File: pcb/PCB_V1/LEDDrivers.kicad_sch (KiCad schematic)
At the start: 65 parts, among them J711 LED +/- (return isolated), J721 LED +/- (return isolated), J731 LED +/- (return isolated), Q711 SiR106ADP-T1-RE3, Q721 DMT10H009LK3-13, Q731 DMT10H009LK3-13, U700 SN74LVC1G08DBVR, U710 AL8853S-13, U720 AL8853S-13, U730 AL8853S-13

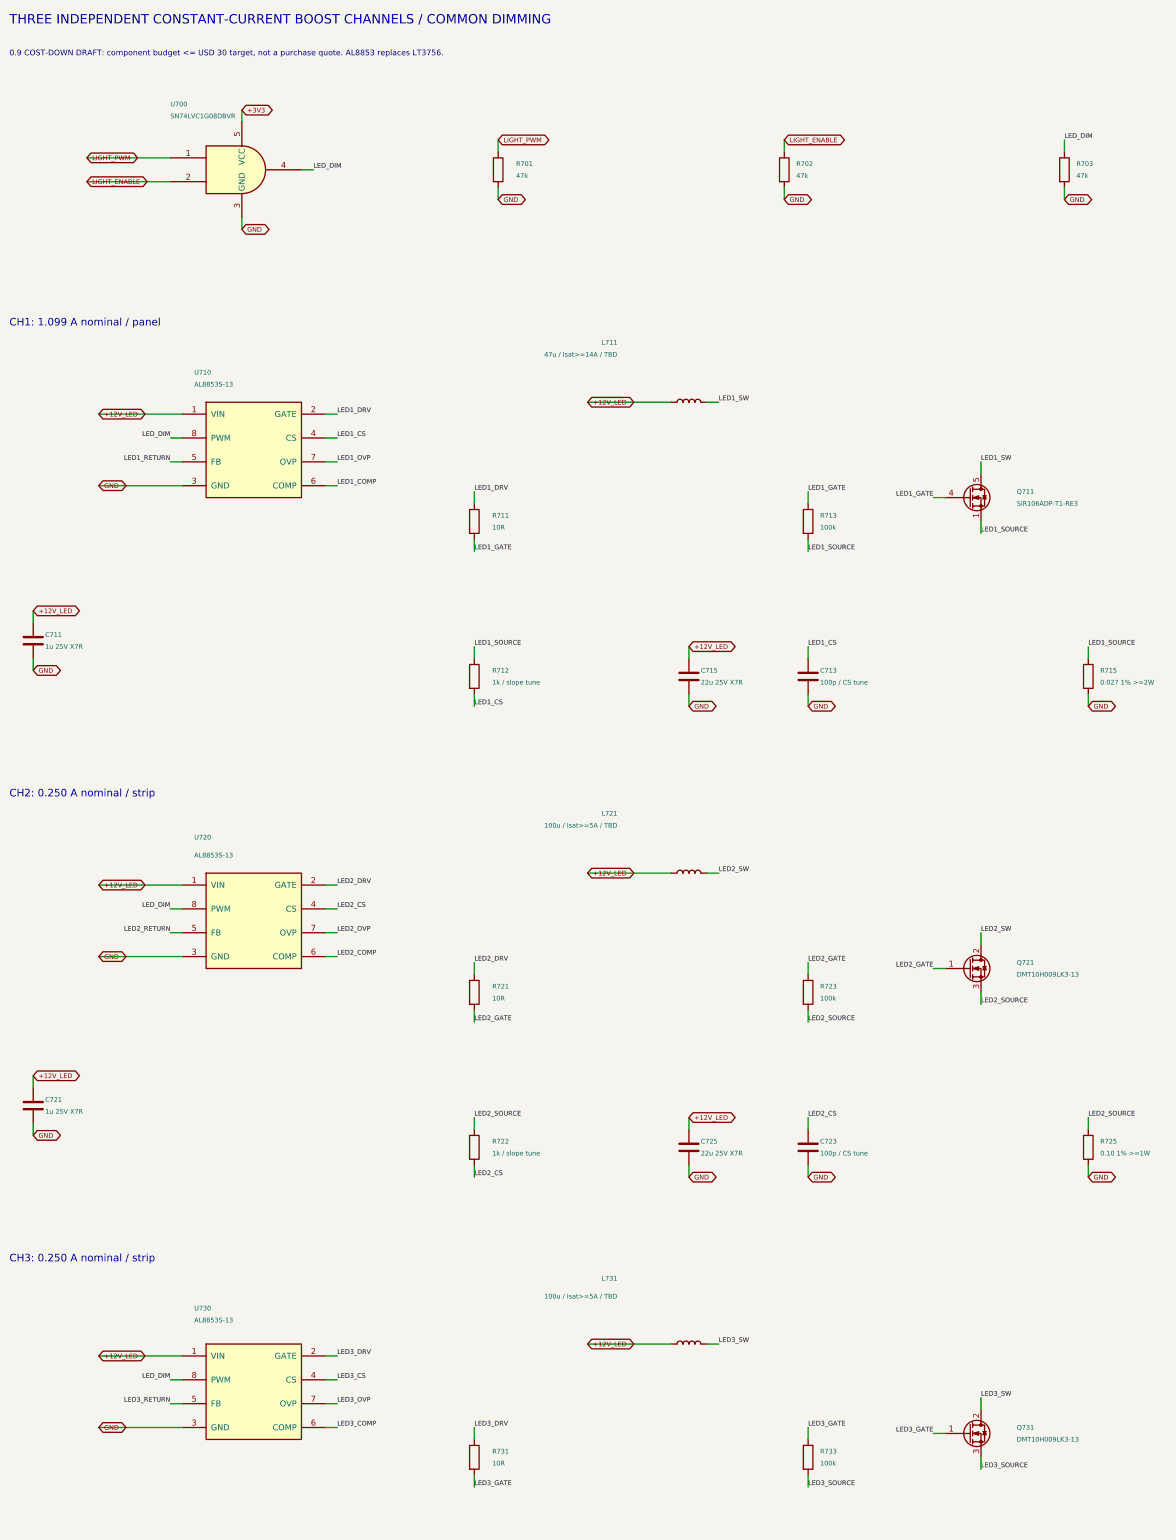
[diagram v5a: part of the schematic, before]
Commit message: pcb: adopt DS3231MZ RTC and compact TI strip MOSFETs
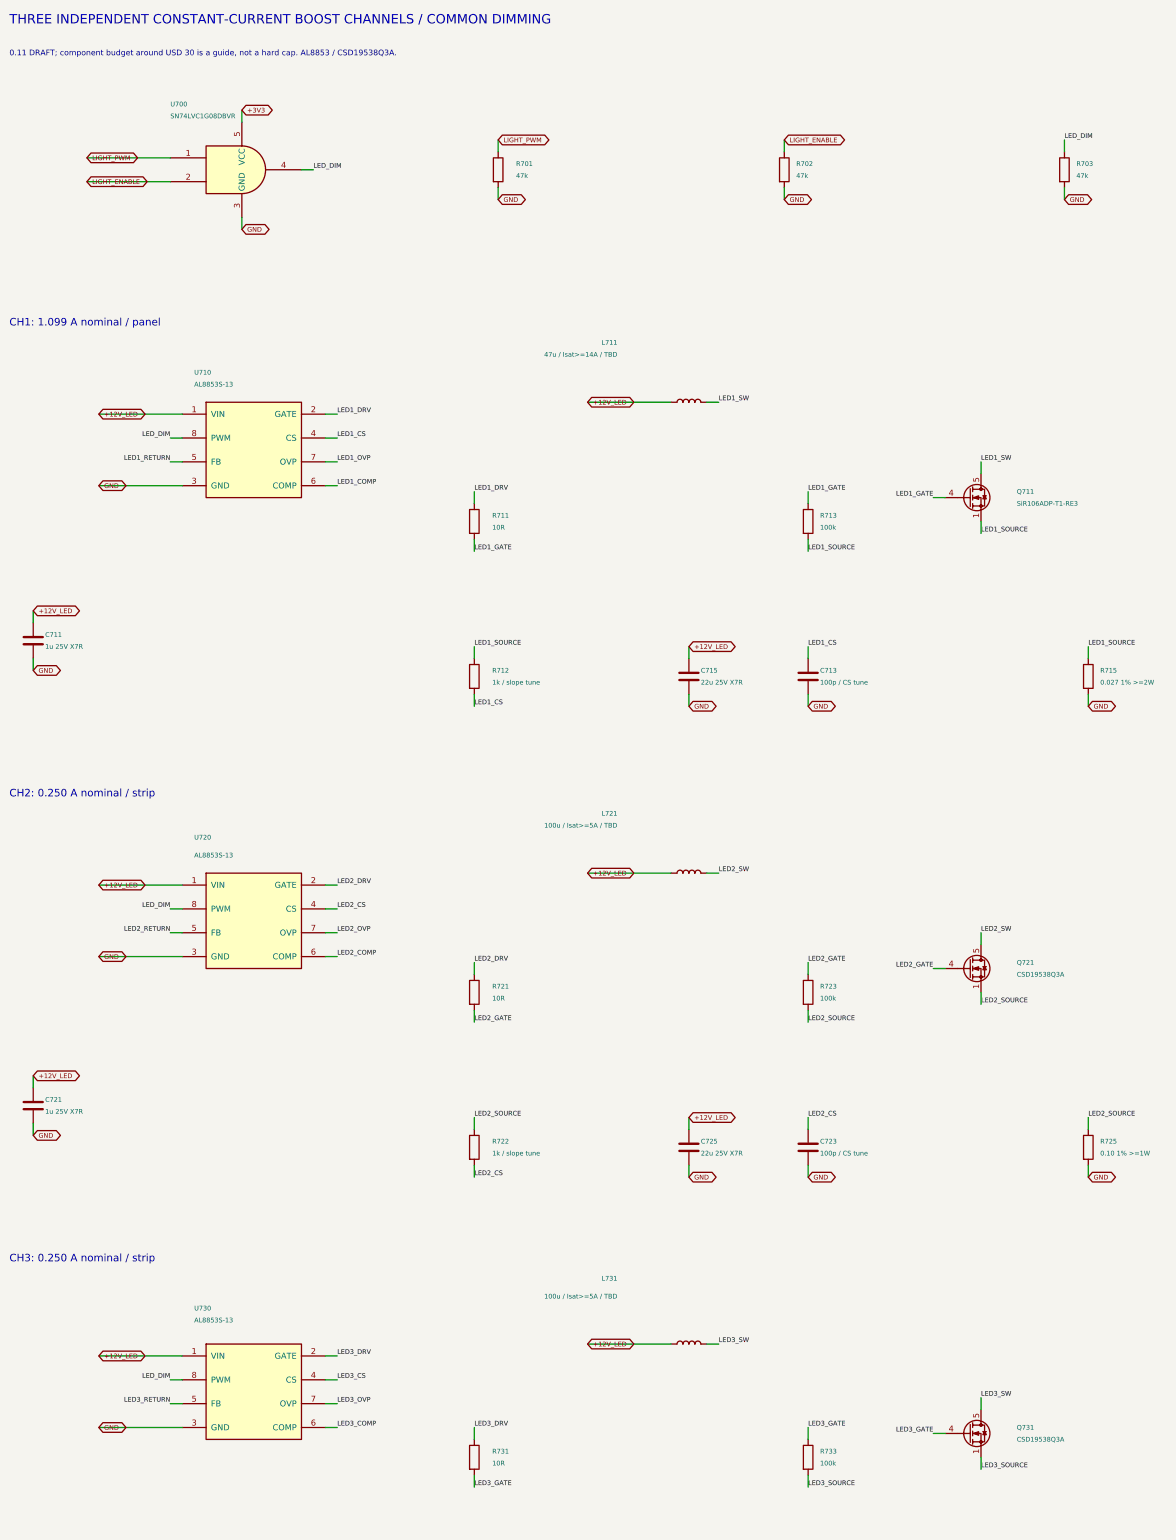
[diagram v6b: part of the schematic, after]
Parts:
- Q721, Q731: value DMT10H009LK3-13 -> CSD19538Q3A; footprint GrowBox:Diodes_TO252_DMT10H009LK3 -> GrowBox:TI_DNH0008A_CSD19538Q3A; symbol GrowBox:DMT10H009LK3 -> GrowBox:CSD19538Q3A
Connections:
- net LED2_GATE: now also Q721.4 (G); no longer Q721.1 (G)
- net LED2_SOURCE: now also Q721.1 (S), Q721.2 (S)
- net LED2_SW: now also Q721.5 (D); no longer Q721.2 (D)
- net LED3_GATE: now also Q731.4 (G); no longer Q731.1 (G)
- net LED3_SOURCE: now also Q731.1 (S), Q731.2 (S)
- net LED3_SW: now also Q731.5 (D); no longer Q731.2 (D)
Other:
- note added: "0.11 DRAFT; component budget around USD 30 is a guide, not a hard cap. AL8853 / CSD19538Q3A."
- note removed: "0.9 COST-DOWN DRAFT: component budget <= USD 30 target, not a purchase quote. AL8853 replaces LT3756."
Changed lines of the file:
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@@
 		(title "07 - AL8853 cost-down LED drivers")
 		(date "2026-09-27")
-		(rev "0.10-DRAFT")
+		(rev "0.11-DRAFT")
 		(company "GrowBox controller")
 		(comment 1 "AL8853 cost-down prototype; not fabrication ready")
@@
 		)
 	)
-	(text "0.9 COST-DOWN DRAFT: component budget <= USD 30 target, not a purchase quote. AL8853 replaces LT3756."
+	(text "0.11 DRAFT; component budget around USD 30 is a guide, not a hard cap. AL8853 / CSD19538Q3A."
 		(exclude_from_sim no)
 		(at 20.32 22.86 0)
@@
 	)
 	(symbol
-		(lib_id "GrowBox:DMT10H009LK3")
+		(lib_id "GrowBox:CSD19538Q3A")
 		(at 224.79 218.44 0)
 		(unit 1)
@@
 			)
 		)
-		(property "Value" "DMT10H009LK3-13"
+		(property "Value" "CSD19538Q3A"
 			(at 234.95 219.71 0)
 			(show_name no)
@@
 			)
 		)
-		(property "Footprint" "GrowBox:Diodes_TO252_DMT10H009LK3"
+		(property "Footprint" "GrowBox:TI_DNH0008A_CSD19538Q3A"
 			(at 224.79 218.44 0)
 			(hide yes)
@@
 			)
 		)
-		(property "Datasheet" "https://www.diodes.com/datasheet/download/DMT10H009LK3.pdf"
+		(property "Datasheet" "https://www.ti.com/lit/ds/symlink/csd19538q3a.pdf"
 			(at 224.79 218.44 0)
 			(hide yes)
@@
 			)
 		)
-		(pin "1"
-		)
-		(pin "2"
-		)
-		(pin "3"
-		)
 		(instances
 			(project "PCB_V1"
@@
 			)
 		)
+		(pin "1"
+		)
+		(pin "2"
+		)
+		(pin "3"
+		)
+		(pin "4"
+		)
+		(pin "5"
+		)
 	)
 	(symbol
@@
 	)
 	(symbol
-		(lib_id "GrowBox:DMT10H009LK3")
+		(lib_id "GrowBox:CSD19538Q3A")
 		(at 224.79 317.5 0)
 		(unit 1)
@@
 			)
 		)
-		(property "Value" "DMT10H009LK3-13"
+		(property "Value" "CSD19538Q3A"
 			(at 234.95 318.77 0)
 			(show_name no)
@@
 			)
 		)
-		(property "Footprint" "GrowBox:Diodes_TO252_DMT10H009LK3"
+		(property "Footprint" "GrowBox:TI_DNH0008A_CSD19538Q3A"
 			(at 224.79 317.5 0)
 			(hide yes)
@@
 			)
 		)
-		(property "Datasheet" "https://www.diodes.com/datasheet/download/DMT10H009LK3.pdf"
+		(property "Datasheet" "https://www.ti.com/lit/ds/symlink/csd19538q3a.pdf"
 			(at 224.79 317.5 0)
 			(hide yes)
@@
 			)
 		)
-		(pin "1"
-		)
-		(pin "2"
-		)
-		(pin "3"
-		)
 		(instances
 			(project "PCB_V1"
@@
 			)
 		)
+		(pin "1"
+		)
+		(pin "2"
+		)
+		(pin "3"
+		)
+		(pin "4"
+		)
+		(pin "5"
+		)
 	)

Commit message: pcb: select LED power passives and add sizing checks
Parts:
- added C718, C719: 10u 100V X7S, Capacitor_SMD:C_1210_3225Metric, symbol Device:C
- C716, C717, C726, C727, C736, C737: value 10u 100V X7R -> 10u 100V X7S; LCSC (none) -> C22380050; MPN (none) -> CL32Y106KCV6PNE; Manufacturer (none) -> Samsung Electro-Mechanics
- D711: value 100V 5A / MPN TBD -> STPS5H100B-TR; footprint Diode_SMD:D_SMC -> Package_TO_SOT_SMD:TO-252-2; symbol Device:D_Schottky -> GrowBox:STPS5H100B; LCSC (none) -> C10648; MPN (none) -> STPS5H100B-TR; Manufacturer (none) -> STMicroelectronics
- D721, D731: value 100V 5A / MPN TBD -> STPS2H100AFY; footprint Diode_SMD:D_SMC -> Diode_SMD:D_SOD-128; LCSC (none) -> C3757915; MPN (none) -> STPS2H100AFY; Manufacturer (none) -> STMicroelectronics
- L711: value 47u / Isat>=14A / TBD -> 47u SRP1770TA-470M; footprint Inductor_SMD:L_Bourns_SRP1245A -> Inductor_SMD:L_Bourns_SRP1770TA_16.9x16.9mm; LCSC (none) -> C2041872; MPN (none) -> SRP1770TA-470M; Manufacturer (none) -> Bourns
- L721, L731: value 100u / Isat>=5A / TBD -> 47u SRP1265A-470M; footprint Inductor_SMD:L_Bourns_SRP1245A -> GrowBox:L_Bourns_SRP1265A; LCSC (none) -> C840530; MPN (none) -> SRP1265A-470M; Manufacturer (none) -> Bourns
- R712: value 1k / slope tune -> 1k 1% / slope tune
- R722, R732: value 1k / slope tune -> 2.7k 1% / slope tune
- R725, R735: value 0.10 1% >=1W -> 0.047 1% >=1W
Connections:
- net GND: now also C718.2, C719.2
- net LED1_OUT: now also D711.2 (K), C718.1, C719.1; no longer D711.1 (K)
- net LED1_SW: now also D711.3 (A); no longer D711.2 (A)
- no-connect marks 0 -> 1
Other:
- note added: "0.12 DRAFT; component budget around USD 30 is a guide, not a hard cap. AL8853 / CSD19538Q3A."
- note added: "216 sizing cases checked; typical ramp only. Startup/OCP, outer-loop stability, hot magnetics and thermal tests remain required."
- note added: "DRAFT: 120 kHz; OVP nominal 65.2 V. 100 V power parts; selected MPNs and sizing: LED_POWER_COMPONENTS.md."
- note removed: "0.11 DRAFT; component budget around USD 30 is a guide, not a hard cap. AL8853 / CSD19538Q3A."
- note removed: "DRAFT: 120 kHz; OVP nominal 65.2 V. All output power parts >=100 V. Inductor/diode footprints are placeholders."
- note removed: "L saturation/current rating, slope compensation, transient response, output capacitance and thermal performance require verification."

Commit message: pcb: add individual branch fuses and qualified terminal geometry
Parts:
- added F711: 10A / 0451010.MRL, GrowBox:Fuse_Littelfuse_451, symbol Device:Fuse
- added F721, F731: 3A / 0451003.MRL, GrowBox:Fuse_Littelfuse_451, symbol Device:Fuse
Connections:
- net +12V_LED: now also F711.1, F721.1, F731.1; no longer C711.1, C715.1, C721.1, C725.1, C731.1, C735.1, L711.1, L721.1, L731.1, U710.1 (VIN), U720.1 (VIN), U730.1 (VIN)
- new net LED1_VIN: C711.1, C715.1, F711.2, L711.1, U710.1 (VIN)
- new net LED2_VIN: C721.1, C725.1, F721.2, L721.1, U720.1 (VIN)
- new net LED3_VIN: C731.1, C735.1, F731.2, L731.1, U730.1 (VIN)
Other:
- note added: "0.14 DRAFT; branch fuses selected, fault clearing and thermal qualification pending."
- note added: "LED- must stay isolated. F711/F721/F731 fuse each INPUT; boost diodes still conduct at shutdown. Verify fault clearing with the actual PSU."
- note removed: "0.12 DRAFT; component budget around USD 30 is a guide, not a hard cap. AL8853 / CSD19538Q3A."
- note removed: "Do not connect LED- to GND or join LED returns. Output short protection needs branch fuses/disconnect; boost diode conducts at shutdown."
